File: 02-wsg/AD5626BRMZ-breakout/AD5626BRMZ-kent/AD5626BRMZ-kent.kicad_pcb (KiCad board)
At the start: 2 copper layers, 17.1 x 12 mm, 7 parts, among them J1 Conn_01x04, J2 Conn_01x04, U1 AD5626BRMZ

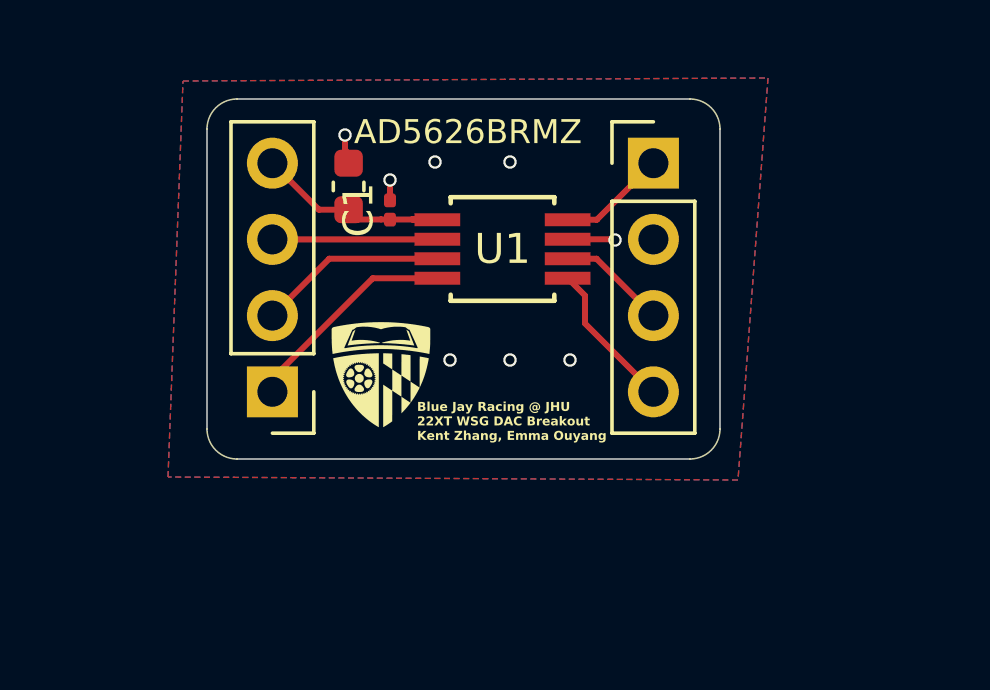
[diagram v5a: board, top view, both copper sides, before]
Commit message: Changed a cap to 0402
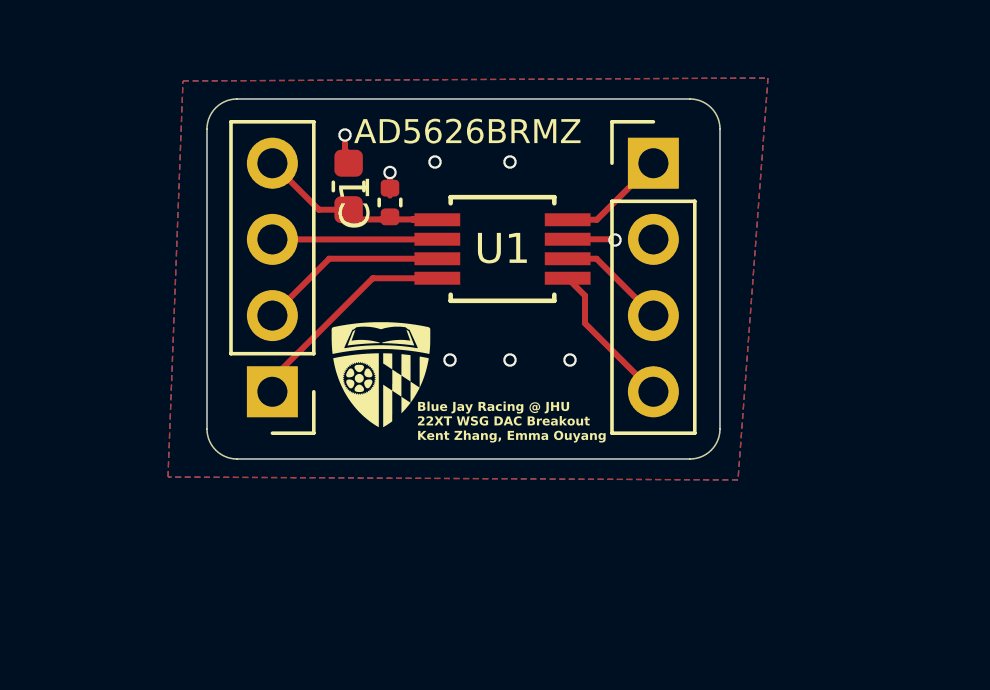
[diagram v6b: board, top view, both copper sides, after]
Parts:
- C1: footprint Capacitor_SMD:C_0201_0603Metric -> Capacitor_SMD:C_0402_1005Metric
- moved C1 0.25 mm to (136.0, 92.8)
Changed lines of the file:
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@@
 		(embedded_fonts no)
 	)
-	(footprint "Capacitor_SMD:C_0201_0603Metric"
-		(layer "F.Cu")
-		(at 136 93 90)
-		(descr "Capacitor SMD 0201 (0603 Metric), square (rectangular) end terminal, IPC-7351 nominal, (Body size source: https://www.vishay.com/docs/20052/crcw0201e3.pdf), generated with kicad-footprint-generator")
+	(footprint "Capacitor_SMD:C_0402_1005Metric"
+		(layer "F.Cu")
+		(at 136 92.75 90)
+		(descr "Capacitor SMD 0402 (1005 Metric), square (rectangular) end terminal, IPC-7351 nominal, (Body size source: IPC-SM-782 page 76, https://www.pcb-3d.com/wordpress/wp-content/uploads/ipc-sm-782a_amendment_1_and_2.pdf), generated with kicad-footprint-generator")
 		(tags "capacitor")
 		(property "Reference" "C1"
-			(at 0 -1.05 90)
+			(at 0 -1.16 90)
 			(layer "F.SilkS")
 			(effects
@@
 		)
 		(property "Value" "0.1uF"
-			(at 0 1.05 90)
+			(at 0 1.16 90)
 			(layer "F.Fab")
 			(effects
@@
 		(attr smd)
 		(fp_line
-			(start 0.7 -0.35)
-			(end 0.7 0.35)
+			(start -0.107836 -0.36)
+			(end 0.107836 -0.36)
+			(stroke
+				(width 0.12)
+				(type solid)
+			)
+			(layer "F.SilkS")
+		)
+		(fp_line
+			(start -0.107836 0.36)
+			(end 0.107836 0.36)
+			(stroke
+				(width 0.12)
+				(type solid)
+			)
+			(layer "F.SilkS")
+		)
+		(fp_line
+			(start 0.91 -0.46)
+			(end 0.91 0.46)
 			(stroke
 				(width 0.05)
@@
 		)
 		(fp_line
-			(start -0.7 -0.35)
-			(end 0.7 -0.35)
+			(start -0.91 -0.46)
+			(end 0.91 -0.46)
 			(stroke
 				(width 0.05)
@@
 		)
 		(fp_line
-			(start 0.7 0.35)
-			(end -0.7 0.35)
+			(start 0.91 0.46)
+			(end -0.91 0.46)
 			(stroke
 				(width 0.05)
@@
 		)
 		(fp_line
-			(start -0.7 0.35)
-			(end -0.7 -0.35)
+			(start -0.91 0.46)
+			(end -0.91 -0.46)
 			(stroke
 				(width 0.05)
@@
 		)
 		(fp_line
-			(start 0.3 -0.15)
-			(end 0.3 0.15)
+			(start 0.5 -0.25)
+			(end 0.5 0.25)
 			(stroke
 				(width 0.1)
@@
 		)
 		(fp_line
-			(start -0.3 -0.15)
-			(end 0.3 -0.15)
+			(start -0.5 -0.25)
+			(end 0.5 -0.25)
 			(stroke
 				(width 0.1)
@@
 		)
 		(fp_line
-			(start 0.3 0.15)
-			(end -0.3 0.15)
+			(start 0.5 0.25)
+			(end -0.5 0.25)
 			(stroke
 				(width 0.1)
@@
 		)
 		(fp_line
-			(start -0.3 0.15)
-			(end -0.3 -0.15)
+			(start -0.5 0.25)
+			(end -0.5 -0.25)
 			(stroke
 				(width 0.1)
@@
 		)
 		(fp_text user "${REFERENCE}"
-			(at 0 -0.68 90)
+			(at 0 0 90)
 			(layer "F.Fab")
 			(effects
@@
 			)
 		)
-		(pad "" smd roundrect
-			(at -0.345 0 90)
-			(size 0.318 0.36)
-			(layers "F.Paste")
-			(roundrect_rratio 0.25)
-		)
-		(pad "" smd roundrect
-			(at 0.345 0 90)
-			(size 0.318 0.36)
-			(layers "F.Paste")
-			(roundrect_rratio 0.25)
-		)
 		(pad "1" smd roundrect
-			(at -0.32 0 90)
-			(size 0.46 0.4)
-			(layers "F.Cu" "F.Mask")
+			(at -0.48 0 90)
+			(size 0.56 0.62)
+			(layers "F.Cu" "F.Mask" "F.Paste")
 			(roundrect_rratio 0.25)
 			(net 7 "Net-(J2-Pin_4)")
@@
 		)
 		(pad "2" smd roundrect
-			(at 0.32 0 90)
-			(size 0.46 0.4)
-			(layers "F.Cu" "F.Mask")
+			(at 0.48 0 90)
+			(size 0.56 0.62)
+			(layers "F.Cu" "F.Mask" "F.Paste")
 			(roundrect_rratio 0.25)
 			(net 8 "GND")
@@
 		)
 		(embedded_fonts no)
-		(model "${KICAD9_3DMODEL_DIR}/Capacitor_SMD.3dshapes/C_0201_0603Metric.step"
+		(model "${KICAD9_3DMODEL_DIR}/Capacitor_SMD.3dshapes/C_0402_1005Metric.step"
 			(offset
 				(xyz 0 0 0)
@@
 	)
 	(segment
-		(start 136 92.52)
-		(end 136 92)
-		(width 0.2)
-		(layer "F.Cu")
-		(net 8)
-	)
-	(segment
 		(start 134.5 90.5)
 		(end 134.5 91)
+		(width 0.2)
+		(layer "F.Cu")
+		(net 8)
+	)
+	(segment
+		(start 136 92.52)
+		(end 136 91.75)
 		(width 0.2)
 		(layer "F.Cu")
@@
 	)
 	(via
-		(at 136 92)
+		(at 136 91.75)
 		(size 0.45)
 		(drill 0.3)
